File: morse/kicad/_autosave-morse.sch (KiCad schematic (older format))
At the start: 10 parts, among them J1 Conn_01x04, Q1 2N2219, Q2 2N2219

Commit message: updating maze symlinks and added rotary encoder to kicad
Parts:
- removed Encoder1: Conn_01x05, Connector_PinHeader_2.54mm:PinHeader_1x05_P2.54mm_Vertical, symbol Connector_Generic:Conn_01x05
- added R3, R4: R, Resistor_THT:R_Axial_DIN0309_L9.0mm_D3.2mm_P12.70mm_Horizontal, symbol Device:R
- added SW1: Rotary_Encoder_Switch, Rotary_Encoder:RotaryEncoder_Alps_EC11E-Switch_Vertical_H20mm_CircularMountingHoles, symbol Device:Rotary_Encoder_Switch
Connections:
- net GND: now also R3.2, R4.2, SW1.C, SW1.S2
- net at Nano1.10 (D7): now also SW1.A
- net at Nano1.11 (D8): now also SW1.B
- net at Nano1.5 (D2), Q1.2 (B): now also R3.1
- net at Nano1.6 (D3), Q2.2 (B): now also R4.1
- net at Nano1.9 (D6): now also SW1.S1
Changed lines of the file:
@@
 Wire Wire Line
 	3500 3550 3500 3250
-$Comp
-L Connector_Generic:Conn_01x05 Encoder1
-U 1 1 61045C91
-P 3150 2600
-F 0 "Encoder1" H 3068 2175 50  0000 C CNN
-F 1 "Conn_01x05" H 3068 2266 50  0000 C CNN
-F 2 "Connector_PinHeader_2.54mm:PinHeader_1x05_P2.54mm_Vertical" H 3150 2600 50  0001 C CNN
-F 3 "~" H 3150 2600 50  0001 C CNN
-	1    3150 2600
-	-1   0    0    1
-$EndComp
-Wire Wire Line
-	3350 2700 3550 2700
-Wire Wire Line
-	3550 2700 3550 2500
-Wire Wire Line
-	3550 2500 3350 2500
-Wire Wire Line
-	3550 2700 3800 2700
-Wire Wire Line
-	3800 2700 3800 3550
-Connection ~ 3550 2700
 Connection ~ 3800 3550
 Wire Wire Line
-	3350 2400 4250 2400
-Wire Wire Line
-	4250 2400 4250 3250
-Wire Wire Line
 	4250 3250 4600 3250
 Wire Wire Line
-	3350 2600 4150 2600
-Wire Wire Line
 	4150 3350 4600 3350
-Wire Wire Line
-	4150 2600 4150 3350
-Wire Wire Line
-	3350 2800 4050 2800
-Wire Wire Line
-	4050 2800 4050 3450
 Wire Wire Line
 	4050 3450 4600 3450
@@
 	6300 4000 6300 4750
 Wire Wire Line
-	6300 4750 5200 4750
+	6300 4750 6000 4750
 Connection ~ 5200 4750
 Wire Wire Line
 	7550 4050 7550 4750
 Wire Wire Line
-	7550 4750 6300 4750
+	7550 4750 7250 4750
 Connection ~ 6300 4750
 Wire Wire Line
@@
 	5100 4250 5200 4250
 Connection ~ 5200 4250
+$Comp
+L Device:R R3
+U 1 1 6108410E
+P 6000 4150
+F 0 "R3" H 6070 4196 50  0000 L CNN
+F 1 "R" H 6070 4105 50  0000 L CNN
+F 2 "Resistor_THT:R_Axial_DIN0309_L9.0mm_D3.2mm_P12.70mm_Horizontal" V 5930 4150 50  0001 C CNN
+F 3 "~" H 6000 4150 50  0001 C CNN
+	1    6000 4150
+	1    0    0    -1
+$EndComp
+$Comp
+L Device:R R4
+U 1 1 61084C3D
+P 7250 4150
+F 0 "R4" H 7320 4196 50  0000 L CNN
+F 1 "R" H 7320 4105 50  0000 L CNN
+F 2 "Resistor_THT:R_Axial_DIN0309_L9.0mm_D3.2mm_P12.70mm_Horizontal" V 7180 4150 50  0001 C CNN
+F 3 "~" H 7250 4150 50  0001 C CNN
+	1    7250 4150
+	1    0    0    -1
+$EndComp
+Wire Wire Line
+	6000 3050 6000 4000
+Connection ~ 6000 3050
+Wire Wire Line
+	7250 4000 7250 3050
+Connection ~ 7250 3050
+Wire Wire Line
+	7250 4300 7250 4750
+Connection ~ 7250 4750
+Wire Wire Line
+	7250 4750 6300 4750
+Wire Wire Line
+	6000 4300 6000 4750
+Connection ~ 6000 4750
+Wire Wire Line
+	6000 4750 5200 4750
+$Comp
+L Device:Rotary_Encoder_Switch SW1
+U 1 1 61085799
+P 3400 2300
+F 0 "SW1" H 3400 2667 50  0000 C CNN
+F 1 "Rotary_Encoder_Switch" H 3400 2576 50  0000 C CNN
+F 2 "Rotary_Encoder:RotaryEncoder_Alps_EC11E-Switch_Vertical_H20mm_CircularMountingHoles" H 3250 2460 50  0001 C CNN
+F 3 "~" H 3400 2560 50  0001 C CNN
+	1    3400 2300
+	1    0    0    -1
+$EndComp
+Wire Wire Line
+	3800 2400 3700 2400
+Wire Wire Line
+	3800 2400 3800 2800
+Wire Wire Line
+	3100 2300 2950 2300
+Wire Wire Line
+	2950 2300 2950 2800
+Wire Wire Line
+	2950 2800 3800 2800
+Connection ~ 3800 2800
+Wire Wire Line
+	3800 2800 3800 3550
+Wire Wire Line
+	4050 2600 3100 2600
+Wire Wire Line
+	3100 2600 3100 2400
+Wire Wire Line
+	4050 2600 4050 3450
+Wire Wire Line
+	4150 1850 2950 1850
+Wire Wire Line
+	2950 1850 2950 2200
+Wire Wire Line
+	2950 2200 3100 2200
+Wire Wire Line
+	4150 1850 4150 3350
+Wire Wire Line
+	3700 2200 4250 2200
+Wire Wire Line
+	4250 2200 4250 3250
 $EndSCHEMATC

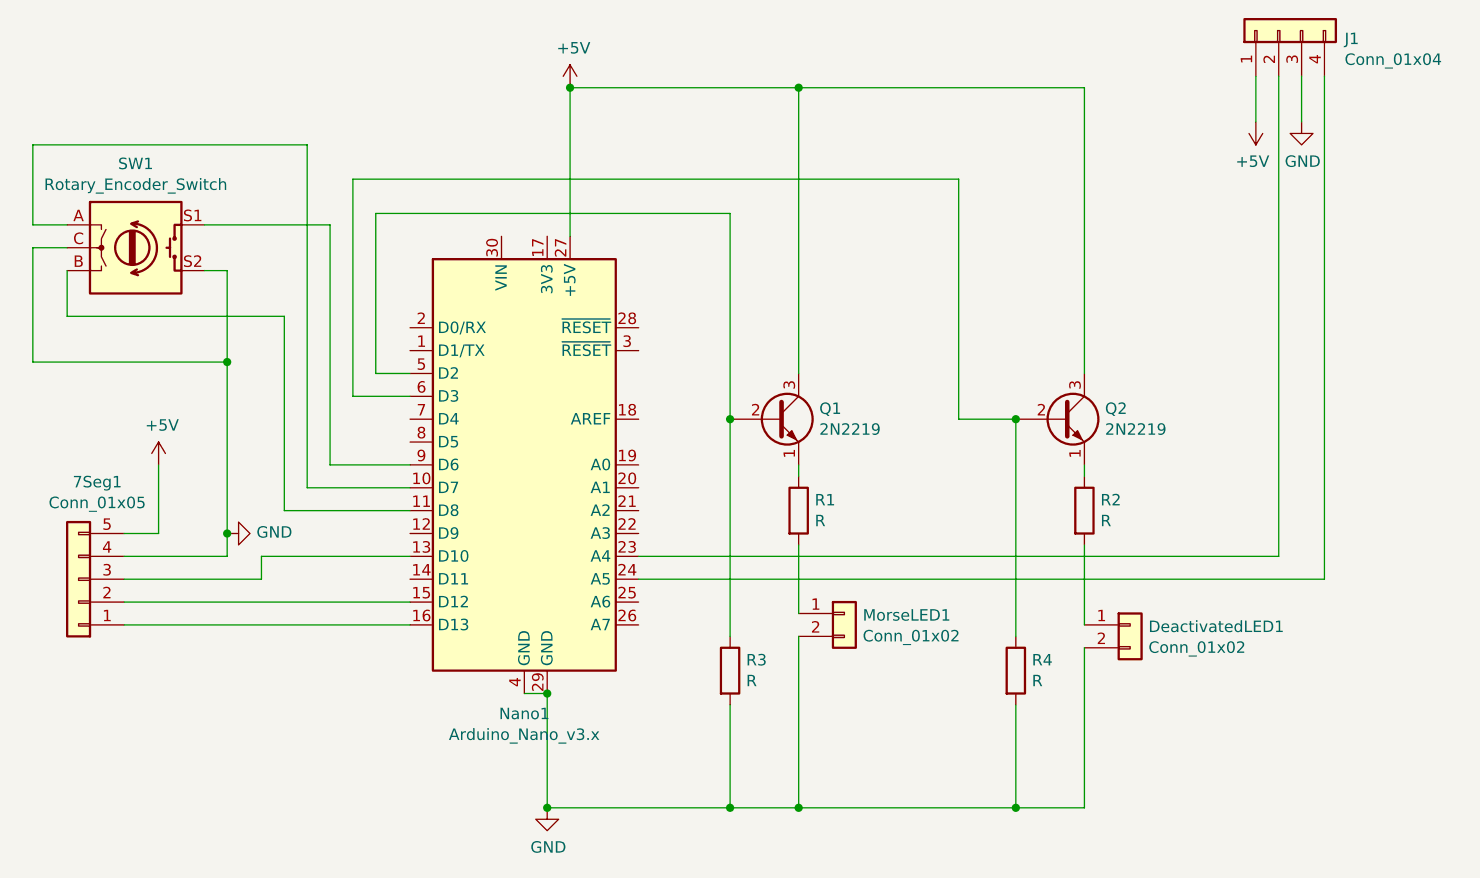
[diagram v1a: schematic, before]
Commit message: started adding knob module, started adding timing into master
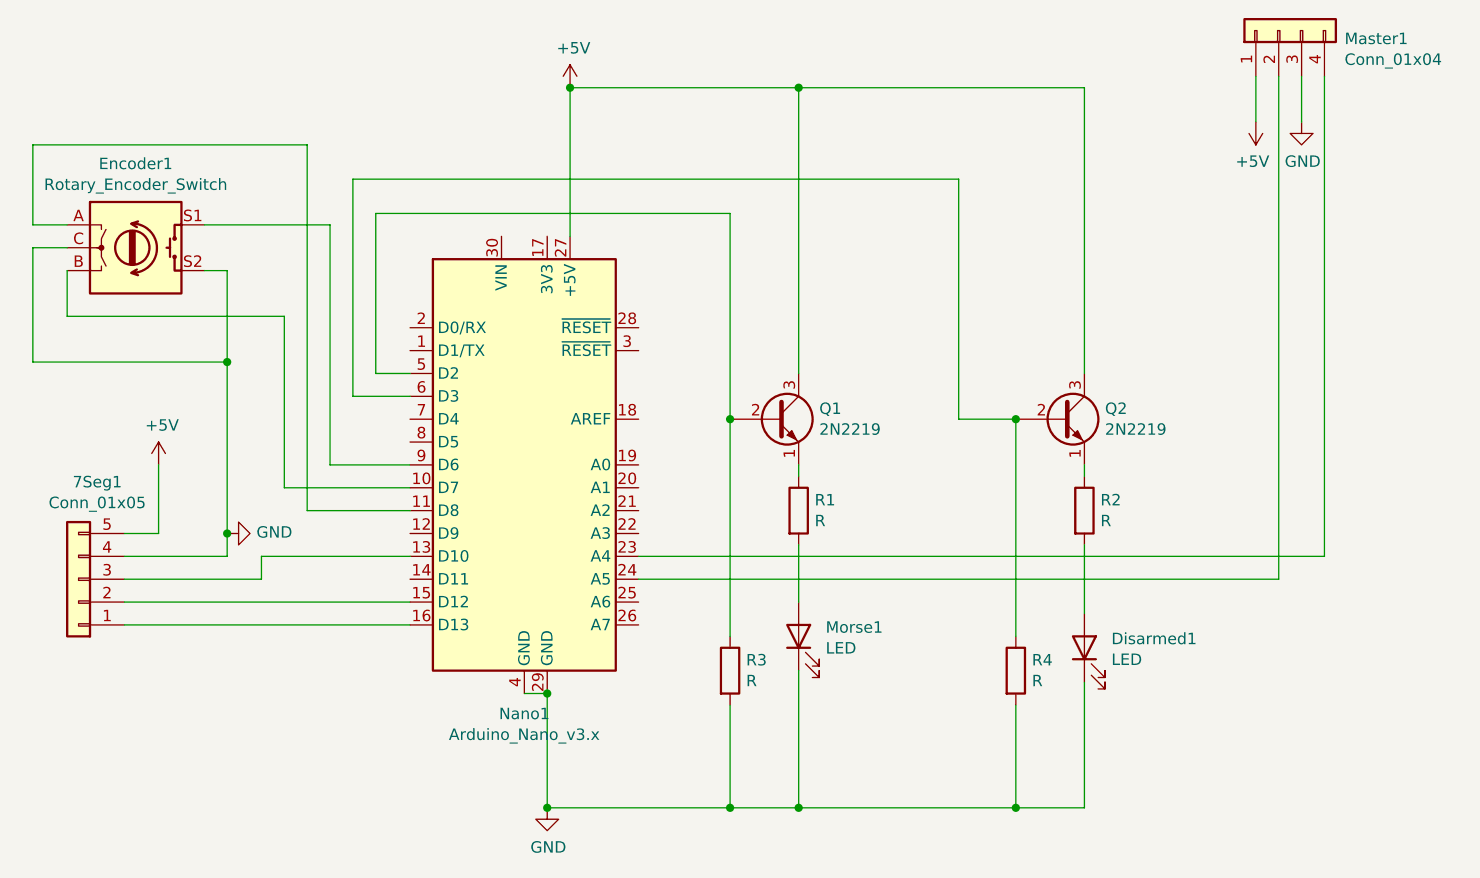
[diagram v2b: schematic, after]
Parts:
- removed DeactivatedLED1, MorseLED1: Conn_01x02, Connector_PinHeader_2.54mm:PinHeader_1x02_P2.54mm_Vertical, symbol Connector_Generic:Conn_01x02
- added Disarmed1: LED, LED_THT:LED_D5.0mm, symbol Device:LED
- added Morse1: LED, LED_THT:LED_D10.0mm, symbol Device:LED
- renumbered SW1 to Encoder1, J1 to Master1
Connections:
- net GND: now also Disarmed1.1 (K), Morse1.1 (K)
- net at Nano1.10 (D7): now also Encoder1.B; no longer Encoder1.A
- net at Nano1.11 (D8): now also Encoder1.A; no longer Encoder1.B
- net at Nano1.23 (A4): now also Master1.4 (Pin_4); no longer Master1.2 (Pin_2)
- net at Nano1.24 (A5): now also Master1.2 (Pin_2); no longer Master1.4 (Pin_4)
- net at R1.2: now also Morse1.2 (A)
- net at R2.2: now also Disarmed1.2 (A)
